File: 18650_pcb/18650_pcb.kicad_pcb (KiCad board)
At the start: 2 copper layers, 40 x 88 mm, 4 parts, among them P1 CONN_01X02

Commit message: More helper&warning text
-Battery connector pinout&wire color codes
-LiIon battery warnings
-"read this before use" clarification
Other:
- board text added: "!"
- board text added: "(black/brown)"
- board text added: "(red/violet)"
- board text added: "--->"
- board text added: "6. Insert microSD and nanoSIM cards 7. Plug charger in, ZeroPhone RGB LED should flash green in 20 seconds or less"
- board text added: "BAT+"
- board text added: "BAT-"
- board text added: "Before use:"
- board text added: "Careful with LiIon batteries - 18650 won't explode, but can burn through wires if you accidentally short them"
- board text removed: "6. Insert microSD and nanoSIM cards 7. Plug charger in, the green LED should flash in 20 seconds or less"
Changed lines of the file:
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@@
     (area 129.924999 55.924999 170.075001 144.075001)
     (thickness 1.6)
-    (drawings 30)
+    (drawings 47)
     (tracks 34)
     (zones 0)
@@
   )
   (setup
-    (last_trace_width 3)
+    (last_trace_width 0.25)
     (user_trace_width 3)
     (trace_clearance 0.2)
@@
       (net 1 "Net-(BT1-Pad1)"))
   )
-  (gr_text "6. Insert microSD and nanoSIM cards\n7. Plug charger in, the green LED \nshould flash in 20 seconds or less" (at 149.23902 126.19324) (layer B.SilkS)
+  (gr_text ---> (at 139.58702 118.82724 110) (layer B.SilkS)
+    (effects (font (size 1.5 1.5) (thickness 0.3)) (justify mirror))
+  )
+  (gr_text ---> (at 160.66902 109.17524 290) (layer B.SilkS)
+    (effects (font (size 1.5 1.5) (thickness 0.3)) (justify mirror))
+  )
+  (gr_text ---> (at 139.84102 109.42924 250) (layer B.SilkS)
+    (effects (font (size 1.5 1.5) (thickness 0.3)) (justify mirror))
+  )
+  (gr_text ---> (at 160.41502 118.57324 70) (layer B.SilkS)
+    (effects (font (size 1.5 1.5) (thickness 0.3)) (justify mirror))
+  )
+  (gr_text "Before use:" (at 162.44702 113.74724) (layer B.SilkS)
+    (effects (font (size 1.5 1.5) (thickness 0.3)) (justify mirror))
+  )
+  (gr_text "Before use:" (at 137.55502 113.74724) (layer B.SilkS)
+    (effects (font (size 1.5 1.5) (thickness 0.3)) (justify mirror))
+  )
+  (gr_line (start 133.99902 136.86124) (end 133.99902 128.47924) (layer B.SilkS) (width 0.2))
+  (gr_line (start 164.47902 136.86124) (end 133.99902 136.86124) (layer B.SilkS) (width 0.2))
+  (gr_line (start 164.47902 128.47924) (end 164.47902 136.86124) (layer B.SilkS) (width 0.2))
+  (gr_line (start 133.99902 128.47924) (end 164.47902 128.47924) (layer B.SilkS) (width 0.2))
+  (gr_text ! (at 137.04702 132.54324) (layer B.SilkS)
+    (effects (font (size 5 5) (thickness 1.25)))
+  )
+  (gr_text ! (at 162.19302 132.54324) (layer B.SilkS)
+    (effects (font (size 5 5) (thickness 1.25)))
+  )
+  (gr_text "Careful with LiIon batteries - \n18650 won't explode, but \ncan burn through wires\nif you accidentally short them" (at 150.00102 132.28924) (layer B.SilkS)
+    (effects (font (size 0.8 0.8) (thickness 0.2)) (justify mirror))
+  )
+  (gr_text BAT+ (at 139.07902 86.31524) (layer B.SilkS)
+    (effects (font (size 1.5 1.5) (thickness 0.3)) (justify mirror))
+  )
+  (gr_text "(red/violet)" (at 135.77702 92.41124) (layer B.SilkS)
+    (effects (font (size 0.8 0.8) (thickness 0.2)) (justify mirror))
+  )
+  (gr_text BAT- (at 139.07902 83.01324) (layer B.SilkS)
+    (effects (font (size 1.5 1.5) (thickness 0.3)) (justify mirror))
+  )
+  (gr_text "(black/brown)" (at 135.77702 76.15524) (layer B.SilkS)
+    (effects (font (size 0.8 0.8) (thickness 0.2)) (justify mirror))
+  )
+  (gr_text "6. Insert microSD and nanoSIM cards\n7. Plug charger in, ZeroPhone RGB LED \nshould flash green in 20 seconds or less" (at 149.23902 125.68524) (layer B.SilkS)
     (effects (font (size 1 1) (thickness 0.25)) (justify mirror))
   )
-  (gr_text "1. Remove microSD and nanoSIM cards\n2. Insert first battery, charge it fully\nthrough microUSB (blue light = full charge)\n3. Remove first battery\n4. Insert second battery, charge fully\n5. Insert first battery" (at 149.74702 99.26924) (layer B.SilkS)
+  (gr_text "1. Remove microSD and nanoSIM cards\n2. Insert first battery, charge it fully\nthrough microUSB (blue light = full charge)\n3. Remove first battery\n4. Insert second battery, charge fully\n5. Insert first battery" (at 150.25502 100.28524) (layer B.SilkS)
     (effects (font (size 1 1) (thickness 0.25)) (justify mirror))
   )

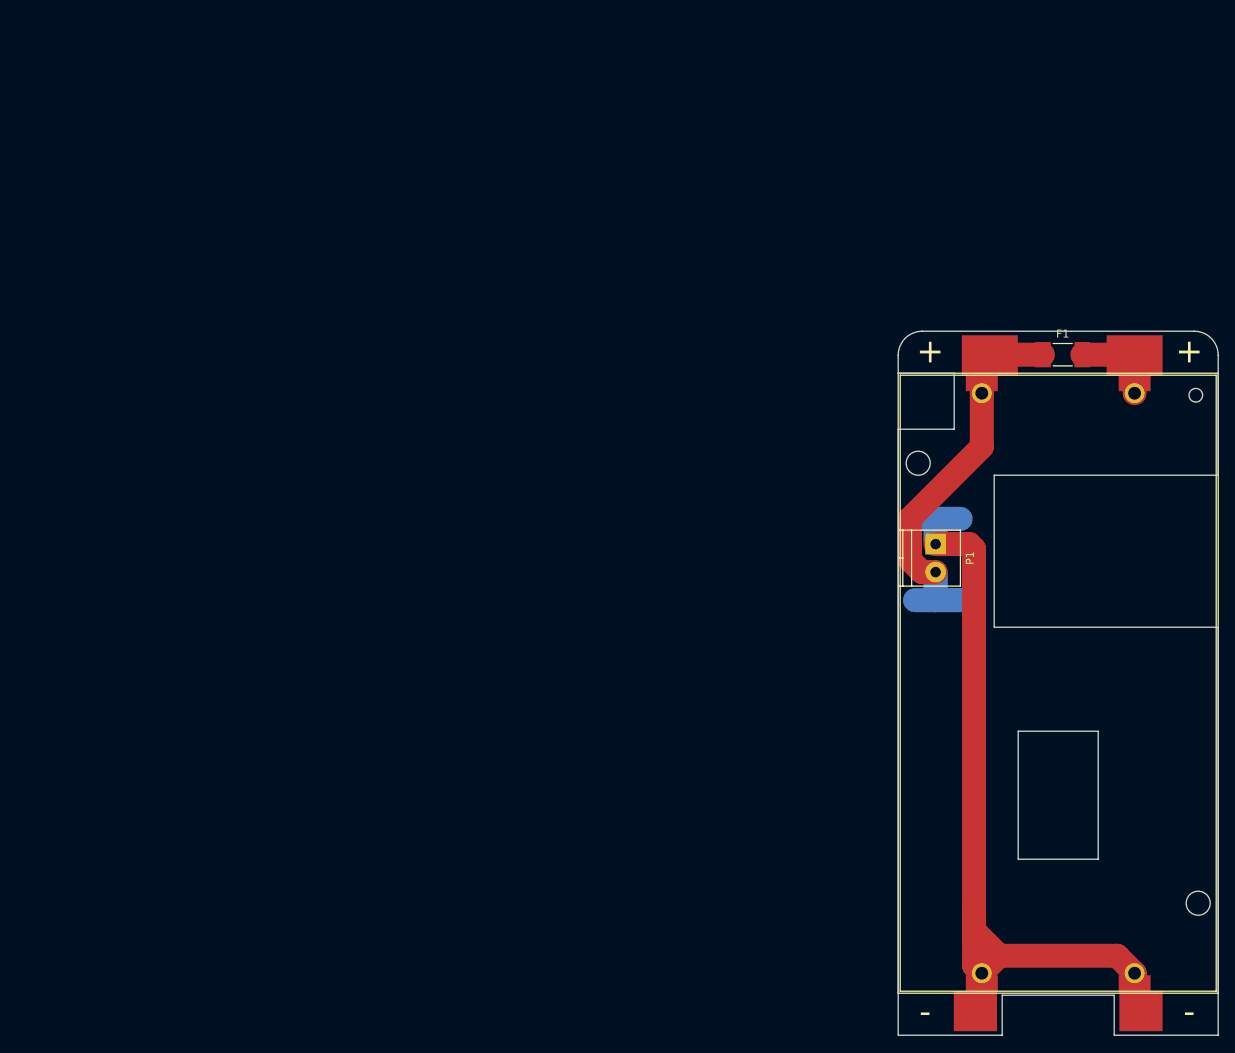
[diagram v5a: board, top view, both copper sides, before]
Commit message: Final changes to 18650 board
-Tweaked outline for better fit
-Added some more text and a little art
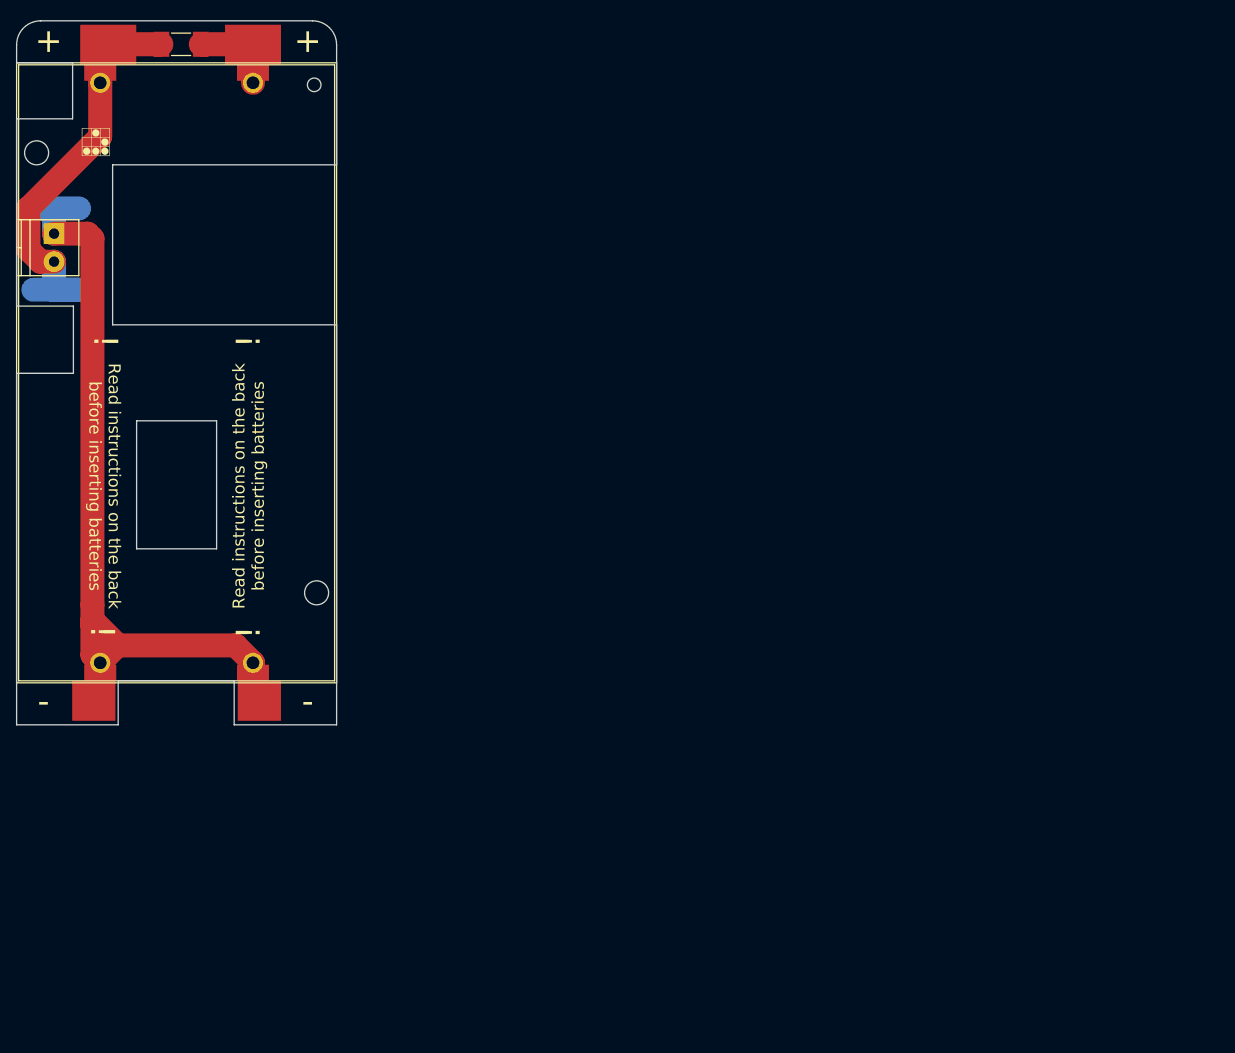
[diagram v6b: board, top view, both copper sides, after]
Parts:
- added G***: LOGO, art:glider, F.Cu at (29.7, 32.4)
- moved BT1 116.8 mm to (39.8, 61.2)
- moved BT2 116.8 mm to (39.8, 61.2)
- moved F1 116.8 mm to (40.4, 20.1)
- moved P1 116.8 mm to (24.5, 43.8)
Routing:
- net Net-(BT1-Pad3): track 110.9 -> 109.0 mm
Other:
- outline, holes or cut-outs redrawn
- board text added: "1. Remove microSD&nanoSIM cards 2. Insert first battery, charge it fully through microUSB (blue light = full) 3. Remove first battery 4. Insert second battery, charge fully 5. Insert first battery"
- board text added: "Read instructions on the back before inserting batteries"
- board text removed: "1. Remove microSD and nanoSIM cards 2. Insert first battery, charge it fully through microUSB (blue light = full charge) 3. Remove first battery 4. Insert second battery, charge fully 5. Insert first battery"

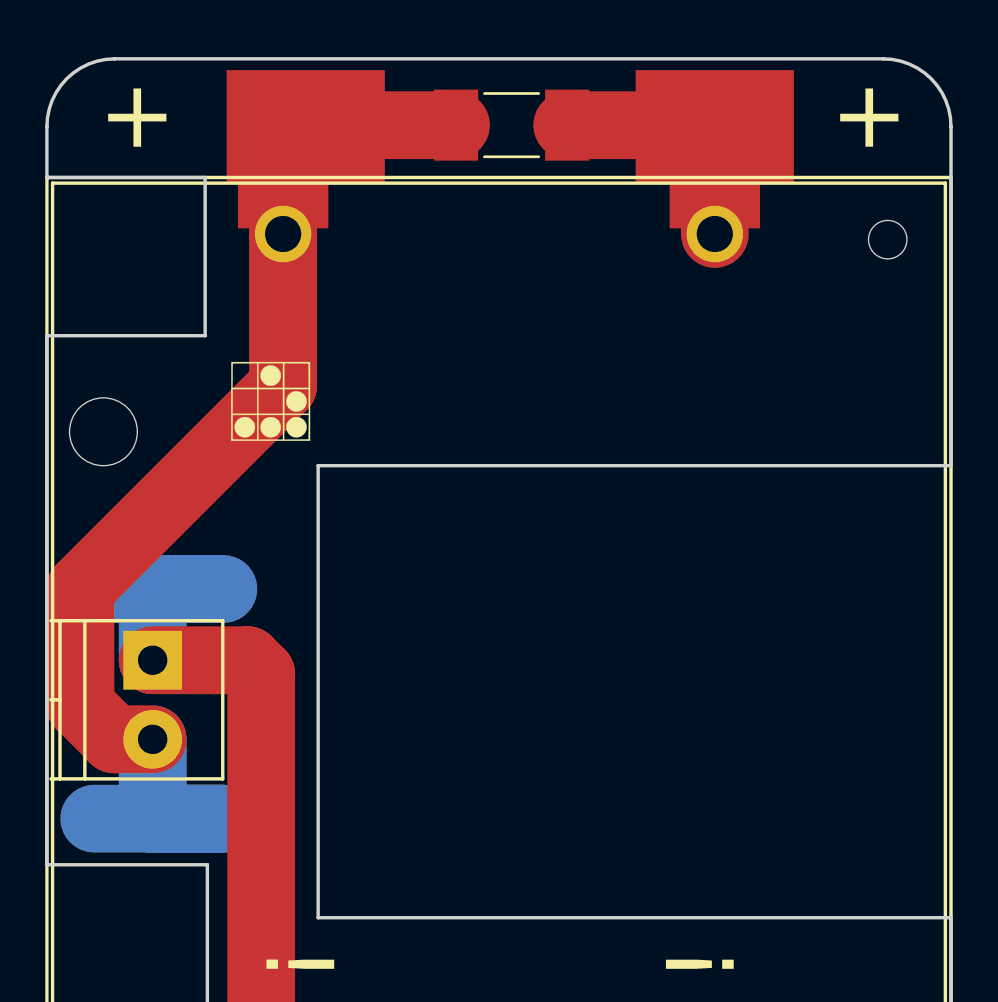
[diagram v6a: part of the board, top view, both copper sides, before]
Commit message: Some more 18650 board fixups
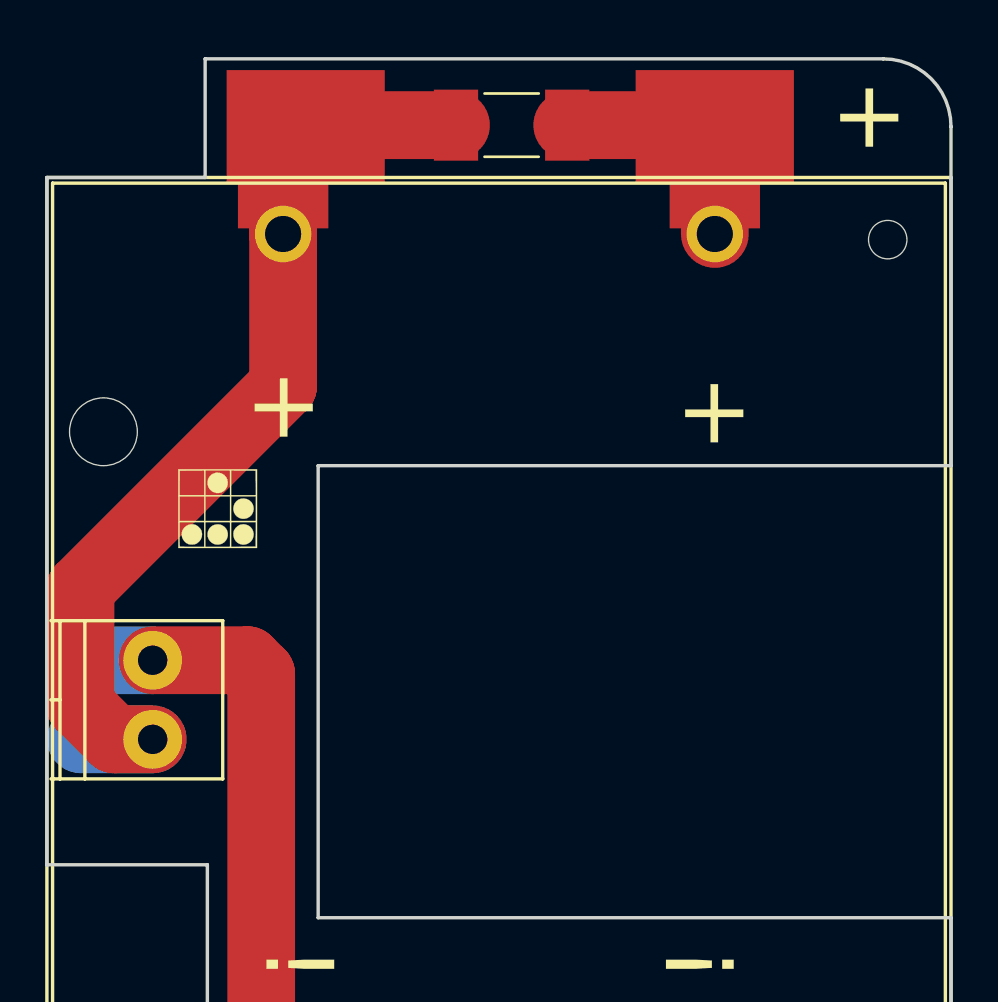
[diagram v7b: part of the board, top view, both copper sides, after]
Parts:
- moved G*** 5.29 mm to (27.4, 37.1)
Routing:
- net Net-(BT1-Pad1): track 52.2 -> 43.0 mm
- net Net-(BT1-Pad3): track 109.0 -> 100.8 mm
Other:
- outline, holes or cut-outs redrawn
- board text added: "(black)"
- board text added: "(red)"
- board text removed: "(black/brown)"
- board text removed: "(red/violet)"
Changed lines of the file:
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@@
-(kicad_pcb (version 4) (host pcbnew 4.0.6)
+(kicad_pcb (version 4) (host pcbnew 4.0.7)
   (general
-    (links 0)
+    (links 13)
     (no_connects 0)
-    (area 17.50362 12.75724 64.39902 105.275001)
+    (area 19.724019 17.124999 59.875001 105.275001)
     (thickness 1.6)
-    (drawings 57)
-    (tracks 33)
+    (drawings 55)
+    (tracks 27)
     (zones 0)
     (modules 5)
@@
       (effects (font (size 1 1) (thickness 0.15)))
     )
-    (fp_text value CONN_01X02 (at 1.75 6 270) (layer F.Fab)
+    (fp_text value CONN_01X02 (at 1.75 6 270) (layer F.Fab) hide
       (effects (font (size 1 1) (thickness 0.15)))
     )
@@
     (pad 2 thru_hole circle (at 3.5 0 270) (size 2.6 2.6) (drill 1.3) (layers *.Cu *.Mask)
       (net 1 "Net-(BT1-Pad1)"))
-    (pad 1 thru_hole rect (at 0 0 270) (size 2.6 2.6) (drill 1.3) (layers *.Cu *.Mask)
+    (pad 1 thru_hole circle (at 0 0 270) (size 2.6 2.6) (drill 1.3) (layers *.Cu *.Mask)
       (net 2 "Net-(BT1-Pad3)"))
   )
@@
   )
   (module art:glider (layer F.Cu)
-    (at 29.69902 32.35724)
+    (at 27.35502 37.10124)
     (fp_text reference G*** (at 0 0) (layer F.SilkS) hide
       (effects (font (thickness 0.3)))
@@
       (xy -0.112592 -1.580121) (xy -0.048089 -1.591067) (xy 0.077808 -1.587251)) (layer F.SilkS) (width 0.01))
   )
+  (gr_text + (at 49.32602 32.78324) (layer F.SilkS)
+    (effects (font (size 3 3) (thickness 0.6)))
+  )
+  (gr_text + (at 30.27602 32.52924) (layer F.SilkS)
+    (effects (font (size 3 3) (thickness 0.6)))
+  )
+  (gr_line (start 26.8 22.45) (end 26.8 17.2) (layer Edge.Cuts) (width 0.15))
   (gr_text ! (at 48.79902 57.25724 90) (layer F.SilkS)
     (effects (font (size 3 3) (thickness 0.75)))
@@
   )
   (gr_line (start 19.79902 61.25724) (end 19.79902 105.2) (layer Edge.Cuts) (width 0.15))
-  (gr_line (start 19.79902 29.45724) (end 19.79902 52.85724) (layer Edge.Cuts) (width 0.15))
+  (gr_line (start 19.79902 22.45) (end 19.79902 52.85724) (layer Edge.Cuts) (width 0.15))
   (gr_line (start 26.89902 61.25724) (end 19.79902 61.25724) (layer Edge.Cuts) (width 0.15))
   (gr_line (start 26.89902 52.85724) (end 26.89902 61.25724) (layer Edge.Cuts) (width 0.15))
@@
     (effects (font (size 1.5 1.5) (thickness 0.3)) (justify mirror))
   )
-  (gr_text "(red/violet)" (at 30.69902 52.35724 90) (layer B.SilkS)
-    (effects (font (size 0.9 0.8) (thickness 0.2)) (justify mirror))
+  (gr_text "(red)" (at 25.06902 50.30924) (layer B.SilkS)
+    (effects (font (size 0.9 0.9) (thickness 0.2)) (justify mirror))
   )
   (gr_text BAT- (at 28.87902 44.21324) (layer B.SilkS)
     (effects (font (size 1.5 1.5) (thickness 0.3)) (justify mirror))
   )
-  (gr_text "(black/brown)" (at 25.57702 37.35524) (layer B.SilkS)
+  (gr_text "(black)" (at 24.94202 40.78424) (layer B.SilkS)
     (effects (font (size 0.9 0.9) (thickness 0.2)) (justify mirror))
   )
@@
     (effects (font (size 3 3) (thickness 0.6)))
   )
-  (gr_text + (at 23.79902 19.70224) (layer F.SilkS)
-    (effects (font (size 3 3) (thickness 0.6)))
-  )
   (gr_text "18650 PCB\nZeroPhone Delta" (at 39.54702 30.49724) (layer B.SilkS)
     (effects (font (size 2 2) (thickness 0.4)) (justify mirror))
@@
   (target plus (at 61.89902 15.25724) (size 5) (width 0.15) (layer Edge.Cuts))
   (gr_line (start 26.8 22.45) (end 19.8 22.45) (layer Edge.Cuts) (width 0.15))
-  (gr_line (start 26.8 22.45) (end 26.8 29.45) (layer Edge.Cuts) (width 0.15))
-  (gr_line (start 19.8 29.45) (end 26.8 29.45) (layer Edge.Cuts) (width 0.15))
   (gr_line (start 34.8 67.2) (end 34.8 83.2) (layer Edge.Cuts) (width 0.15))
   (gr_line (start 34.8 83.2) (end 44.8 83.2) (layer Edge.Cuts) (width 0.15))
@@
   (gr_line (start 31.8 35.2) (end 31.8 55.2) (layer Edge.Cuts) (width 0.15))
   (gr_line (start 31.8 35.2) (end 59.8 35.2) (layer Edge.Cuts) (width 0.15))
-  (gr_arc (start 22.8 20.2) (end 19.8 20.2) (angle 90) (layer Edge.Cuts) (width 0.15))
   (gr_arc (start 56.8 20.2) (end 56.8 17.2) (angle 90) (layer Edge.Cuts) (width 0.15))
-  (gr_line (start 19.8 22.45) (end 19.8 20.2) (layer Edge.Cuts) (width 0.15))
   (gr_line (start 32.5 105.2) (end 19.8 105.2) (layer Edge.Cuts) (width 0.15))
   (gr_line (start 32.5 99.7) (end 32.5 105.2) (layer Edge.Cuts) (width 0.15))
@@
   (gr_line (start 59.8 105.2) (end 47 105.2) (layer Edge.Cuts) (width 0.15))
   (gr_line (start 59.8 35.2) (end 59.8 20.2) (layer Edge.Cuts) (width 0.15))
-  (gr_line (start 22.8 17.2) (end 56.8 17.2) (layer Edge.Cuts) (width 0.15))
-  (segment (start 27.60902 50.81724) (end 21.89402 50.81724) (width 3) (layer B.Cu) (net 1))
-  (segment (start 24.43402 50.81724) (end 27.60902 50.81724) (width 3) (layer B.Cu) (net 1))
-  (segment (start 24.47862 50.77264) (end 24.43402 50.81724) (width 3) (layer B.Cu) (net 1))
-  (segment (start 24.47862 47.30804) (end 24.47862 50.77264) (width 3) (layer B.Cu) (net 1))
+  (gr_line (start 26.8 17.2) (end 56.8 17.2) (layer Edge.Cuts) (width 0.15))
+  (segment (start 24.47862 47.30804) (end 21.30582 47.30804) (width 3) (layer B.Cu) (net 1))
   (segment (start 37.89982 20.13404) (end 31.31596 20.13404) (width 3) (layer F.Cu) (net 1))
   (segment (start 31.31596 20.13404) (end 31.25 20.2) (width 3) (layer F.Cu) (net 1))
@@
   (segment (start 22.781564 47.30804) (end 21.27861 45.805086) (width 3) (layer F.Cu) (net 1))
   (segment (start 30.25 20.2) (end 30.25 24.95) (width 3) (layer F.Cu) (net 1))
+  (segment (start 24.47862 43.80804) (end 21.28322 43.80804) (width 3) (layer B.Cu) (net 2))
   (segment (start 29.27862 90.18724) (end 29.27862 92.72724) (width 3) (layer F.Cu) (net 2))
   (segment (start 29.27862 44.40804) (end 29.27862 90.18724) (width 3) (layer F.Cu) (net 2))
@@
   (segment (start 32.43276 95.26724) (end 47.16724 95.26724) (width 3) (layer F.Cu) (net 2))
   (segment (start 30.25 97.45) (end 32.43276 95.26724) (width 3) (layer F.Cu) (net 2))
-  (segment (start 21.89402 40.65724) (end 27.60902 40.65724) (width 3) (layer B.Cu) (net 2))
-  (segment (start 24.43402 40.65724) (end 21.89402 40.65724) (width 3) (layer B.Cu) (net 2))
-  (segment (start 24.47862 40.70184) (end 24.43402 40.65724) (width 3) (layer B.Cu) (net 2))
-  (segment (start 24.47862 43.80804) (end 24.47862 40.70184) (width 3) (layer B.Cu) (net 2))
   (segment (start 24.47862 43.80804) (end 28.67862 43.80804) (width 3) (layer F.Cu) (net 2))
   (segment (start 28.67862 43.80804) (end 29.27862 44.40804) (width 3) (layer F.Cu) (net 2))
@@
     (polygon
       (pts
-        (xy 19.98902 38.75224) (xy 30.14902 38.75224) (xy 30.14902 42.56224) (xy 19.98902 42.56224)
+        (xy 19.86202 45.73724) (xy 26.08502 45.73724) (xy 26.08502 48.78524) (xy 19.86202 48.78524)
       )
     )
@@
     (polygon
       (pts
-        (xy 19.98902 48.91224) (xy 30.14902 48.91224) (xy 30.14902 52.72224) (xy 19.98902 52.72224)
+        (xy 19.73502 42.18124) (xy 26.08502 42.18124) (xy 26.08502 45.35624) (xy 19.73502 45.35624)
       )
     )
